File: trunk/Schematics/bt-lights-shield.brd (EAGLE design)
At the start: 76.3 x 80 mm, 27 parts, among them IC1 MAX6966, U1 ARDUINO_SHIELDNO_SILK

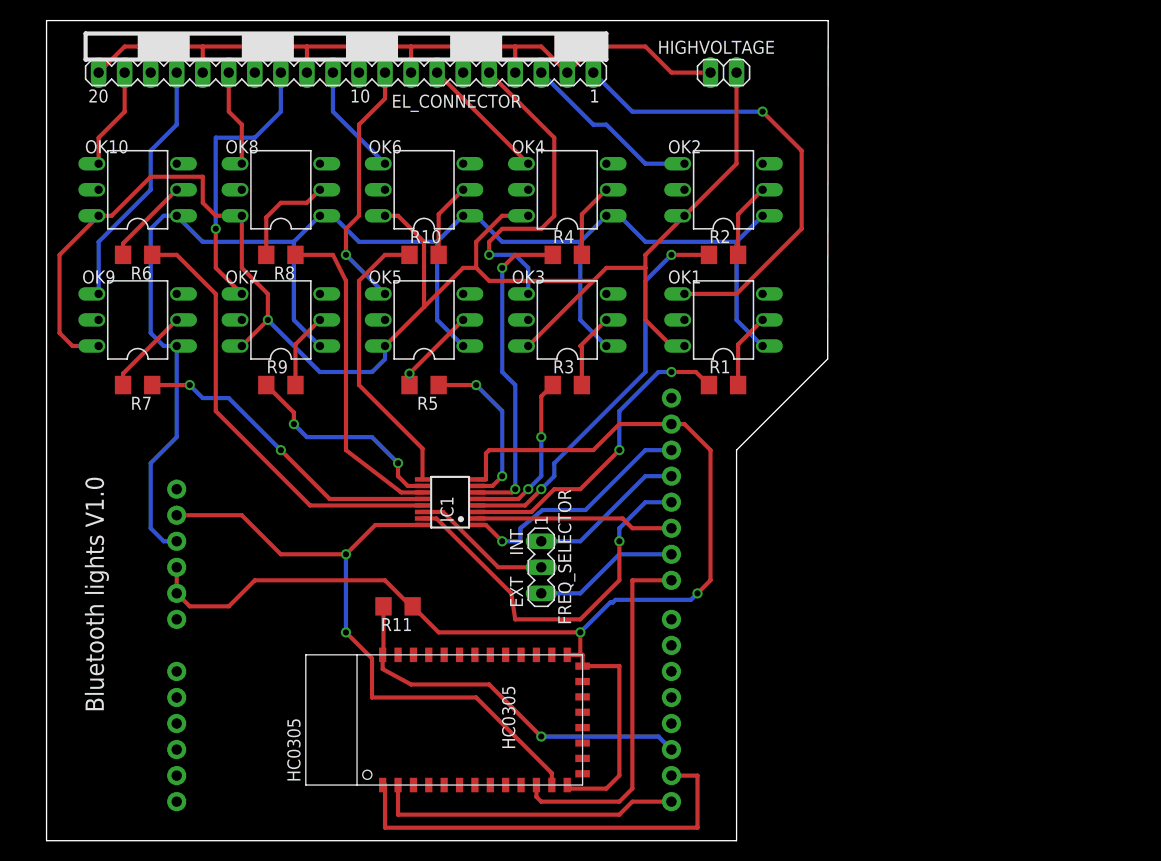
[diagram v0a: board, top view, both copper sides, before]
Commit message: Update App for setup view
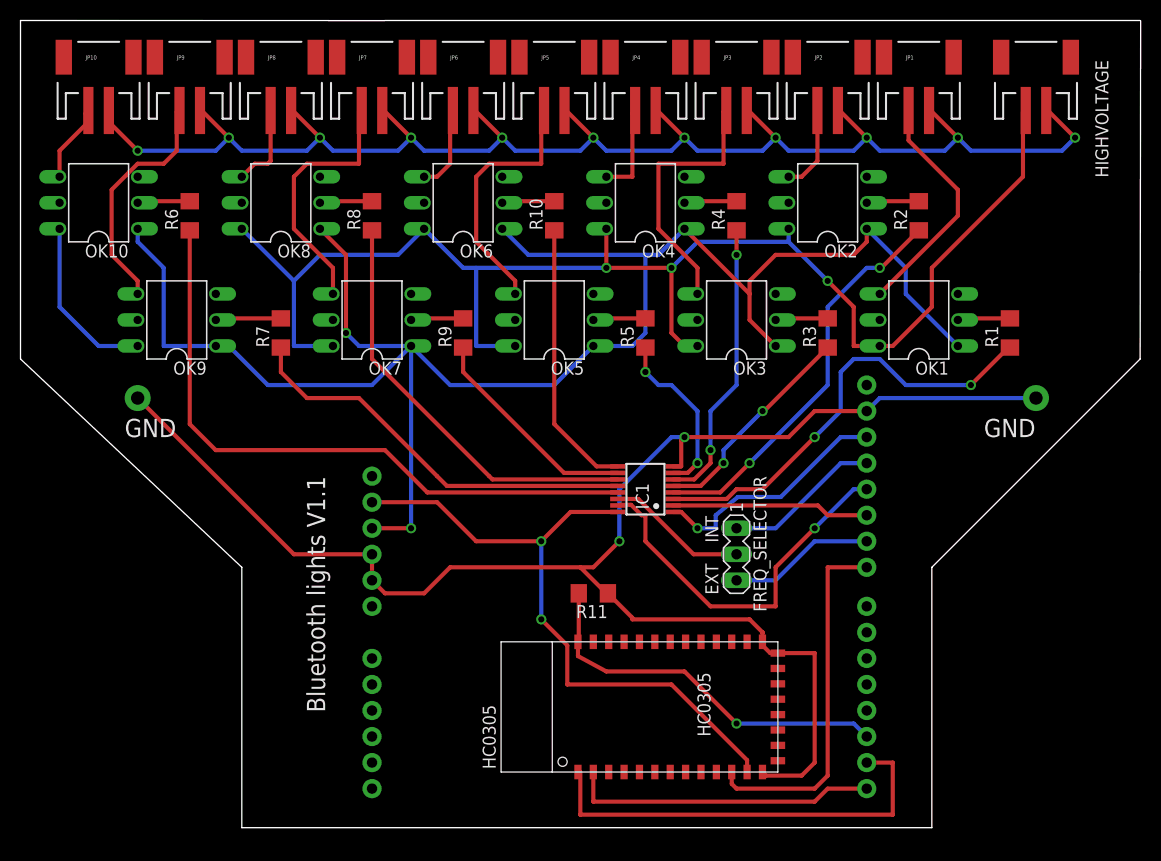
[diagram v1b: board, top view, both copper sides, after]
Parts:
- removed EL_CONNECTOR: (no value), con-lstb:MA20-1L
- added JP1, JP10, JP2, JP3, JP4, JP5, JP6, JP7, JP8, JP9: (no value), SparkFun-Connectors:JST-2-SMD
- HIGHVOLTAGE: device pinhead:1X02 -> SparkFun-Connectors:JST-2-SMD
- moved HIGHVOLTAGE 30.5 mm to (96.5, 74.9)
- moved R1 28.4 mm to (94.0, 49.5), turned to 90 degrees
- moved R3 25.9 mm to (76.2, 49.5), turned to 90 degrees
- moved R5 22.2 mm to (58.4, 49.5), turned to 90 degrees
- moved R2 19.4 mm to (85.1, 61.0), turned to 90 degrees
- moved FREQ_SELECTOR 19.1 mm to (67.3, 27.9)
- moved HC0305 19.1 mm to (53.3, 12.7)
- moved IC1 19.1 mm to (58.4, 34.3)
- moved R11 19.1 mm to (53.3, 24.1)
- moved U1 19.1 mm to (82.5, 47.0)
- moved OK1 19.0 mm to (85.1, 50.8)
- moved R9 18.5 mm to (40.6, 49.5), turned to 90 degrees
- moved R4 16.9 mm to (67.3, 61.0), turned to 90 degrees
- moved OK3 16.5 mm to (67.3, 50.8)
- moved R7 14.9 mm to (22.9, 49.5), turned to 90 degrees
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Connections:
- net N$P1 renamed IN1
- net N$P2 renamed IN2
- net N$P3 renamed IN3
- net N$P4 renamed IN4
- net N$P5 renamed IN5
- net N$P6 renamed IN6
- net N$P7 renamed IN7
- net N$P8 renamed IN8
- net N$P9 renamed IN9
- net OUT0: now also JP1.1; no longer EL_CONNECTOR.1
- net OUT1: now also JP2.1; no longer EL_CONNECTOR.3
- net OUT2: now also JP3.1; no longer EL_CONNECTOR.5
- net OUT3: now also JP4.1; no longer EL_CONNECTOR.7
- net OUT4: now also JP5.1; no longer EL_CONNECTOR.9
- net OUT5: now also JP6.1; no longer EL_CONNECTOR.11
- net OUT6: now also JP7.1; no longer EL_CONNECTOR.13
- net OUT7: now also JP8.1; no longer EL_CONNECTOR.15
- net OUT8: now also JP9.1; no longer EL_CONNECTOR.17
- net OUT9: now also JP10.1; no longer EL_CONNECTOR.19
- net VDD: now also HIGHVOLTAGE.2, JP1.2, JP10.2, JP2.2, JP3.2, JP4.2, JP5.2, JP6.2, JP7.2, JP8.2, JP9.2; no longer EL_CONNECTOR.10, EL_CONNECTOR.12, EL_CONNECTOR.14, EL_CONNECTOR.16, EL_CONNECTOR.18, EL_CONNECTOR.2, EL_CONNECTOR.20, EL_CONNECTOR.4, EL_CONNECTOR.6, EL_CONNECTOR.8, HIGHVOLTAGE.1
- net VSS: now also HIGHVOLTAGE.1; no longer HIGHVOLTAGE.2
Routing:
- net VDD: track 84.2 -> 145.6 mm, vias 0 -> 11
- net GND: track 125.4 -> 155.3 mm, vias 2 -> 4
- net +5V: track 149.9 -> 179.3 mm, vias 0 -> 2
- net OUT0: track 45.2 -> 23.0 mm, vias 1 -> 0
- net IN9: track 43.2 -> 63.6 mm
- net IN0: track 31.0 -> 43.4 mm
- net IN7: track 31.9 -> 41.4 mm
- net OUT1: track 17.7 -> 8.37 mm
- net IN8: track 31.0 -> 39.9 mm, vias 2 -> 0
- net OUT2: track 32.1 -> 26.0 mm, vias 1 -> 0
- net IN2: track 16.5 -> 21.4 mm
- net N$8: track 10.0 -> 5.14 mm
- net OUT3: track 12.6 -> 9.11 mm
- net N$6: track 8.52 -> 5.14 mm
- net N$14: track 8.52 -> 5.14 mm, vias 1 -> 0
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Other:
- board size 76.3 x 80 mm -> 109.3 x 78.7 mm
- board text added: "Bluetooth lights V1.1"
- board text added: "GND"
- board text removed: "Bluetooth lights V1.0"
